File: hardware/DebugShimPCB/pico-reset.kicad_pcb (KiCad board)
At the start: 2 copper layers, 21.2 x 51.3 mm, 3 parts, among them J2 PINHD_1x3_Female, SW1 Push_Button

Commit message: generate gerbers, add credit
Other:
- board text added: "Debug Shim V1.0 by V205"
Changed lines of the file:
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@@
       (outputformat 1)
       (mirror false)
-      (drillshape 1)
+      (drillshape 0)
       (scaleselection 1)
       (outputdirectory "")
@@
   (gr_rect (start 110.018969 79.748257) (end 131.211302 131.048242)
     (stroke (width 0.1) (type default)) (fill none) (layer "Edge.Cuts"))
+  (gr_text "Debug Shim V1.0\nby V205" (at 127.67815 130.132808) (layer "B.SilkS")
+    (effects (font (size 1 1) (thickness 0.15)) (justify left bottom mirror))
+  )
   (segment (start 115.713135 81.28) (end 116.524152 82.091017) (width 0.25) (layer "B.Cu") (net 1))
   (segment (start 111.76 81.28) (end 115.713135 81.28) (width 0.25) (layer "B.Cu") (net 1))

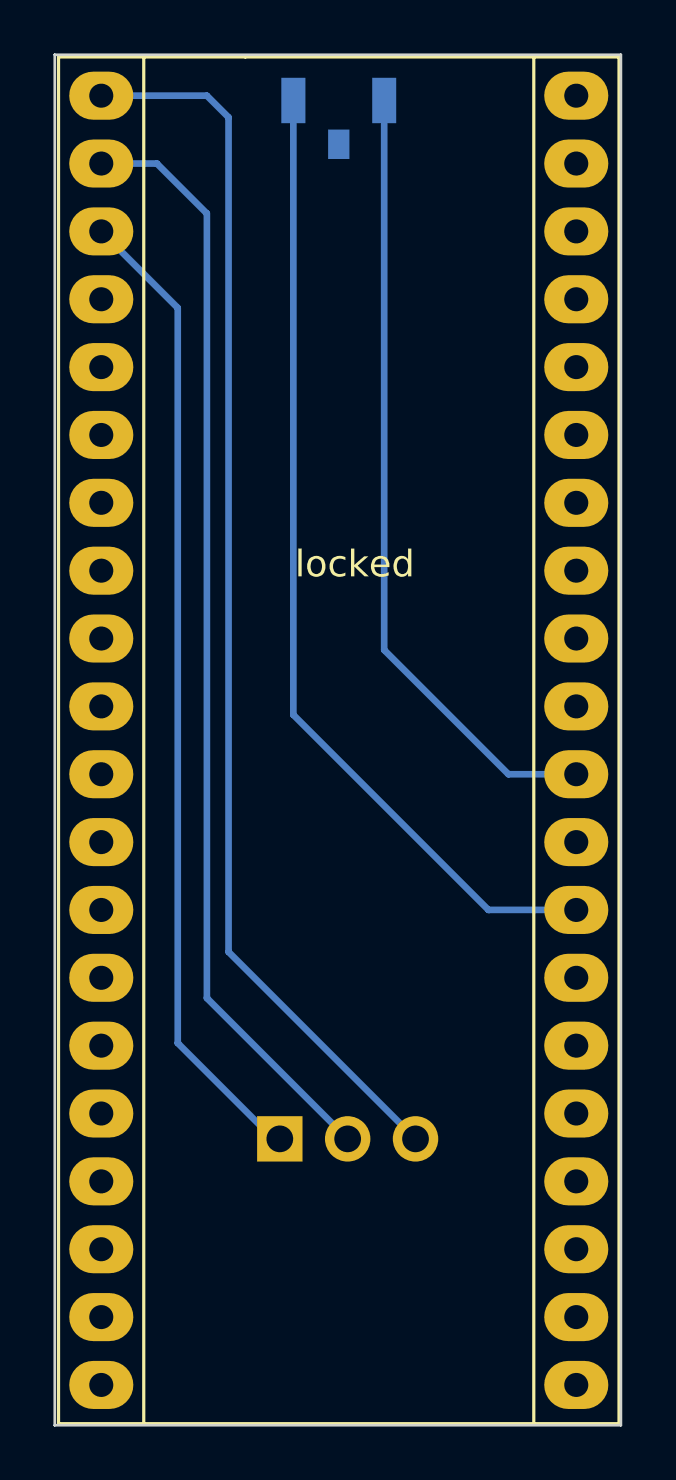
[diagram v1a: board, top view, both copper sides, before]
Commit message: update hole size (again..)
update holes on shim to be tighter fit to headers.
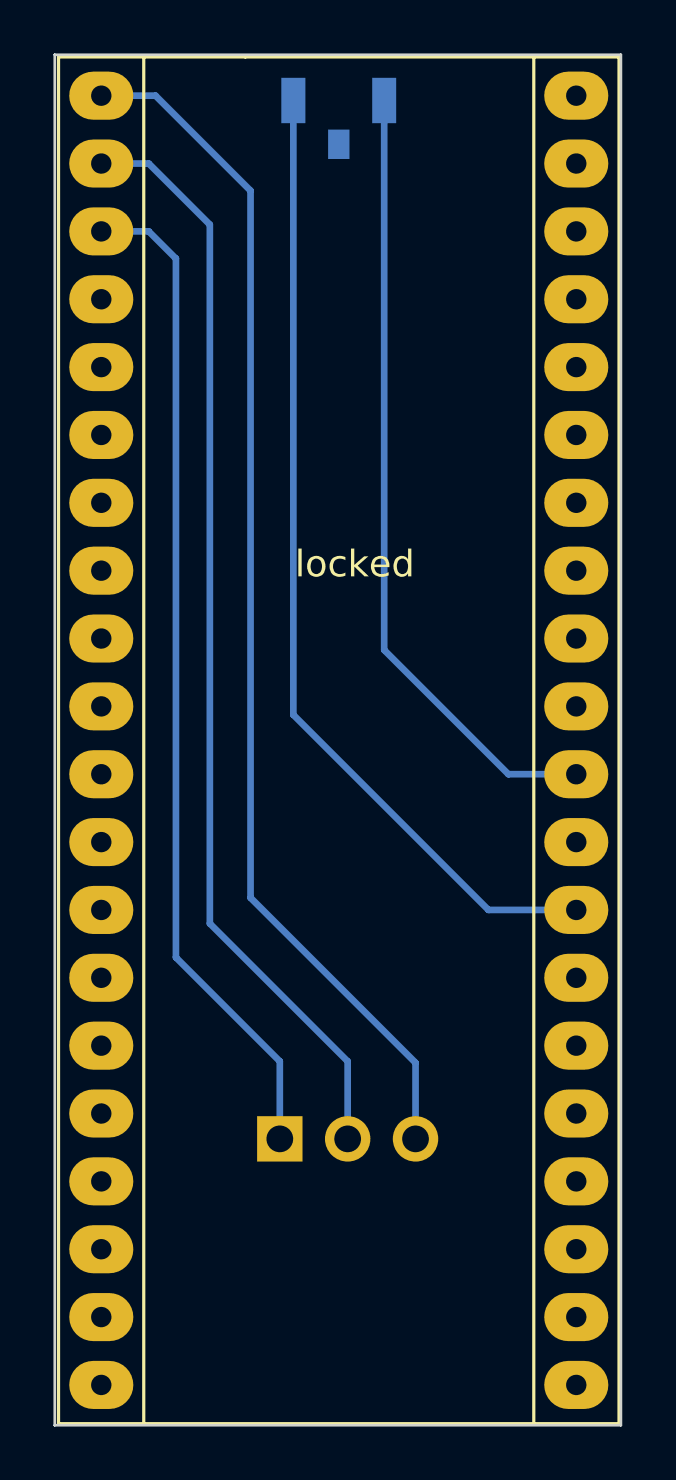
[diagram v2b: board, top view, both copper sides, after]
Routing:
- net Net-(A1-GP0): track 46.2 -> 45.1 mm
- net GND: track 36.9 -> 37.8 mm
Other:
- board text added: "Debug Shim V1.1 by V205"
- board text removed: "Debug Shim V1.0 by V205"
